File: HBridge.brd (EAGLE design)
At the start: 59.7 x 53.3 mm, 42 parts, among them IC1 74HC08D, IC2 A4954, J1 In 1/2, J2 In 3/4

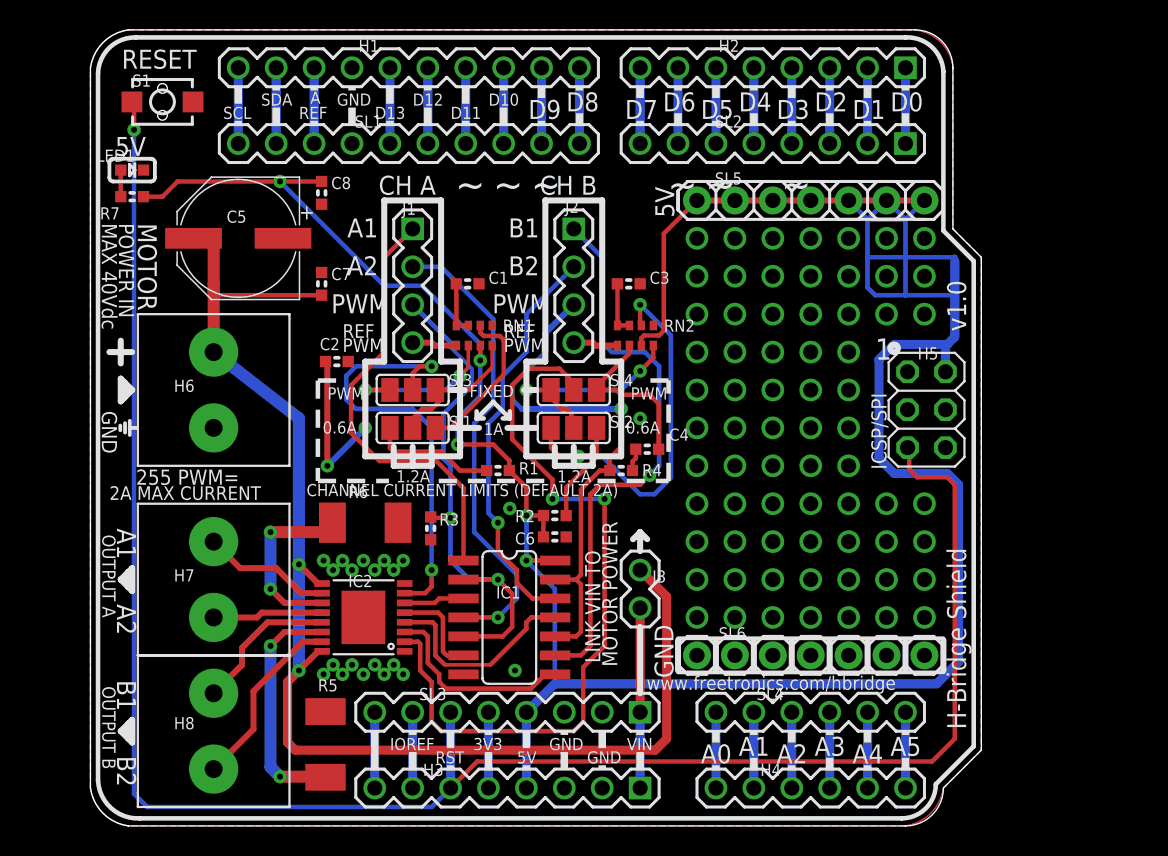
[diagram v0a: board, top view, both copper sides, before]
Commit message: Restructured schematic and board for switchable current limit
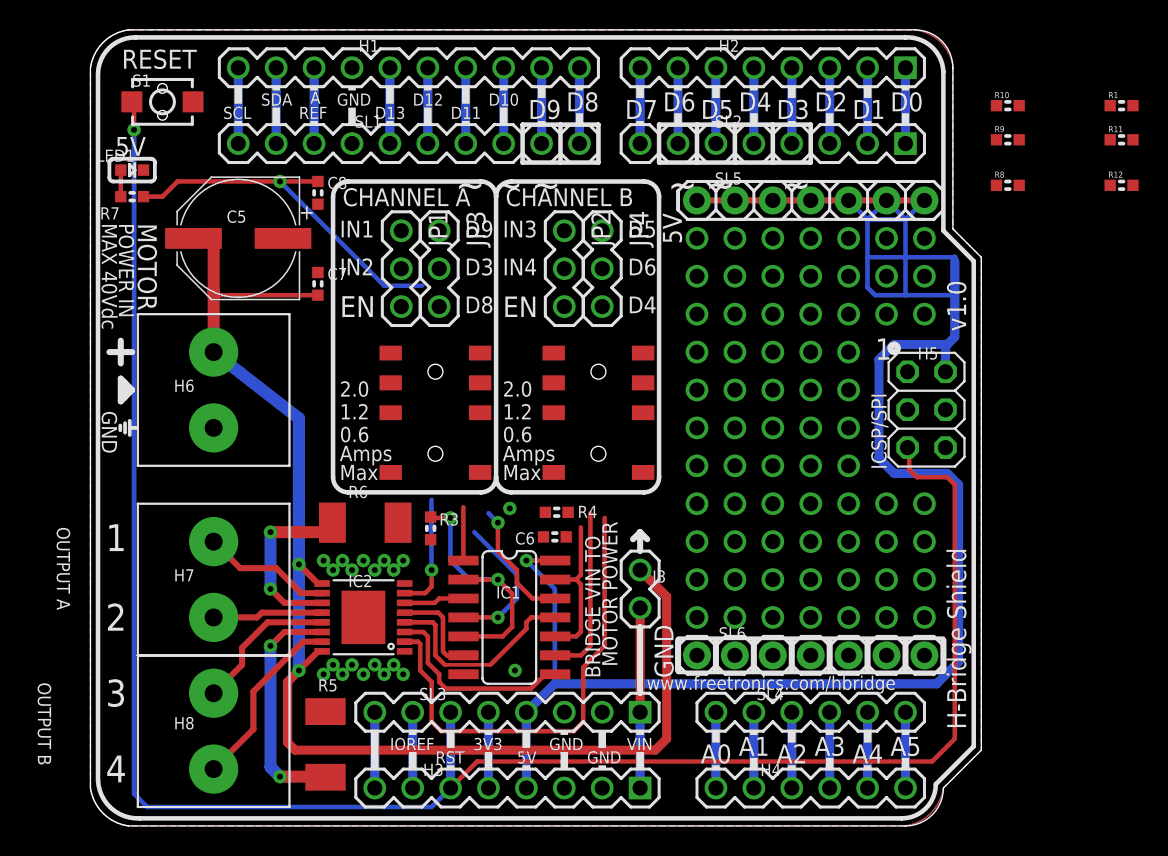
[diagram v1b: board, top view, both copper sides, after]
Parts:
- removed C1, C2, C3, C4: 100nF, freetronics-master-v1:0603
- removed J1: In 1/2, freetronics-master-v1:1X04
- removed J2: In 3/4, freetronics-master-v1:1X04
- removed R2: 2K2, freetronics-master-v1:0603
- removed RN1, RN2: 1K, freetronics-master-v1:CAY16
- removed SJ1: Ch1 Fixed Current Select, freetronics-master-v1:SJ_2
- removed SJ2: Ch2 Fixed Current Select, freetronics-master-v1:SJ_2
- removed SJ3: Ch1 Fixed/PWM select, freetronics-master-v1:SJ_2
- removed SJ4: Ch2 Fixed/PWM select, freetronics-master-v1:SJ_2
- added JP1, JP2, JP3, JP4: (no value), freetronics-master-v1.1:1X03
- added R10: 3K3, freetronics-master-v1:0603
- added R11, R9: 953R, freetronics-master-v1:0603
- added R12, R8: 2K2, freetronics-master-v1:0603
- added SW1, SW2: SWITCH-DP3T, freetronics-jon:MS-23C01
- R1: value 2K2 -> 3K3
- moved R1 48.4 mm to (69.1, 48.3)
- moved R4 5.14 mm to (31.2, 21.0)
- moved C7 0.25 mm to (15.2, 36.3)
- moved C8 0.25 mm to (15.2, 42.4)
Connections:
- removed net N$1: RN2.4, SJ2.2, SJ4.3
- removed net N$16: RN1.4, SJ1.2, SJ3.3
- removed net N$17: R2.1, SJ2.1
- removed net N$18: C2.1, RN1.2, SJ3.1
- removed net N$19: C1.1, RN1.7, RN1.8
- removed net N$2: C4.1, RN2.2, SJ4.1
- removed net N$20: RN2.6, SJ2.3
- removed net N$3: C3.1, RN2.7, RN2.8
- removed net PWM12: IC1.2, IC1.5, J1.3, R3.2
- removed net PWM34: IC1.10, IC1.13, J2.3, R4.2
- removed net REF_PWM_12: J1.4, RN1.1
- removed net REF_PWM_34: J2.4, RN2.1
- new net EN-A: IC1.2, IC1.5, JP1.3, R3.2
- new net EN-B: IC1.10, IC1.13, JP2.3, R4.1
- new net N$21: R9.1, SW1.2-3
- new net N$49: R1.1, SW2.2-2
- net +5V: now also R12.1, R3.1, R4.2, R8.1; no longer R1.2, R2.2, RN1.3, RN2.3
- net D3: now also JP3.2
- net D4: now also JP4.3
- net D5: now also JP4.1
- net D6: now also JP4.2
- net D8: now also JP3.3
- net D9: now also JP3.1
- net GND: now also R1.2, R10.2, R11.2, R9.2; no longer C1.2, C2.2, C3.2, C4.2, R3.1, R4.1, RN1.5, RN2.5
- net IN1: now also JP1.1; no longer J1.1
- net IN2: now also JP1.2; no longer J1.2
- net IN3: now also JP2.1; no longer J2.1
- net IN4: now also JP2.2; no longer J2.2
- net N$15: now also R10.1, SW1.2-2; no longer RN1.6, SJ1.3
- net N$4: now also R11.1, SW2.2-3; no longer R1.1, SJ1.1
- net VREF12: now also R8.2, SW1.2-C; no longer SJ3.2
- net VREF34: now also R12.2, SW2.2-C; no longer SJ4.2
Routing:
- net +5V: track 194.5 -> 154.9 mm, vias 5 -> 2
- net PWM12: track 35.6 -> 0.00 mm, vias 2 -> 0
- net PWM34: track 35.6 -> 0.00 mm, vias 1 -> 0
- net IN3: track 37.7 -> 11.5 mm, vias 1 -> 0
- net IN1: track 29.3 -> 3.58 mm
- net N$20: track 25.0 -> 0.00 mm, vias 2 -> 0
- net N$18: track 23.9 -> 0.00 mm, vias 4 -> 0
- net IN2: track 31.4 -> 9.74 mm
- net VREF12: track 29.3 -> 7.80 mm, vias 2 -> 1
- net VREF34: track 50.5 -> 31.6 mm, vias 2 -> 0
- net IN4: track 27.3 -> 8.46 mm
- net EN-A: track 0.00 -> 18.7 mm, vias 0 -> 2
- net N$1: track 15.2 -> 0.00 mm, vias 2 -> 0
- net N$2: track 11.8 -> 0.00 mm
- net N$15: track 10.6 -> 0.00 mm
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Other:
- board text added: "0.6"
- board text added: "1.2"
- board text added: "2"
- board text added: "2.0"
- board text added: "3"
- board text added: "4"
- board text added: "Amps"
- board text added: "BRIDGE VIN TO"
- board text added: "CHANNEL A"
- board text added: "CHANNEL B"
- board text added: "EN"
- board text added: "IN1"
- board text added: "IN2"
- board text added: "IN3"
- board text added: "IN4"
- board text added: "Max"
- board text removed: "0.6A"
- board text removed: "1.2A"
- board text removed: "1A"
- board text removed: "255 PWM="
- board text removed: "2A MAX CURRENT"
- board text removed: "B1"
- board text removed: "B2"
- board text removed: "CH A"
- board text removed: "CH B"
- board text removed: "CHANNEL CURRENT LIMITS (DEFAULT 2A)"
- board text removed: "FIXED"
- board text removed: "LINK VIN TO"
- board text removed: "PWM"

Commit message: Changed input pins; rerouted; ERC and DRC
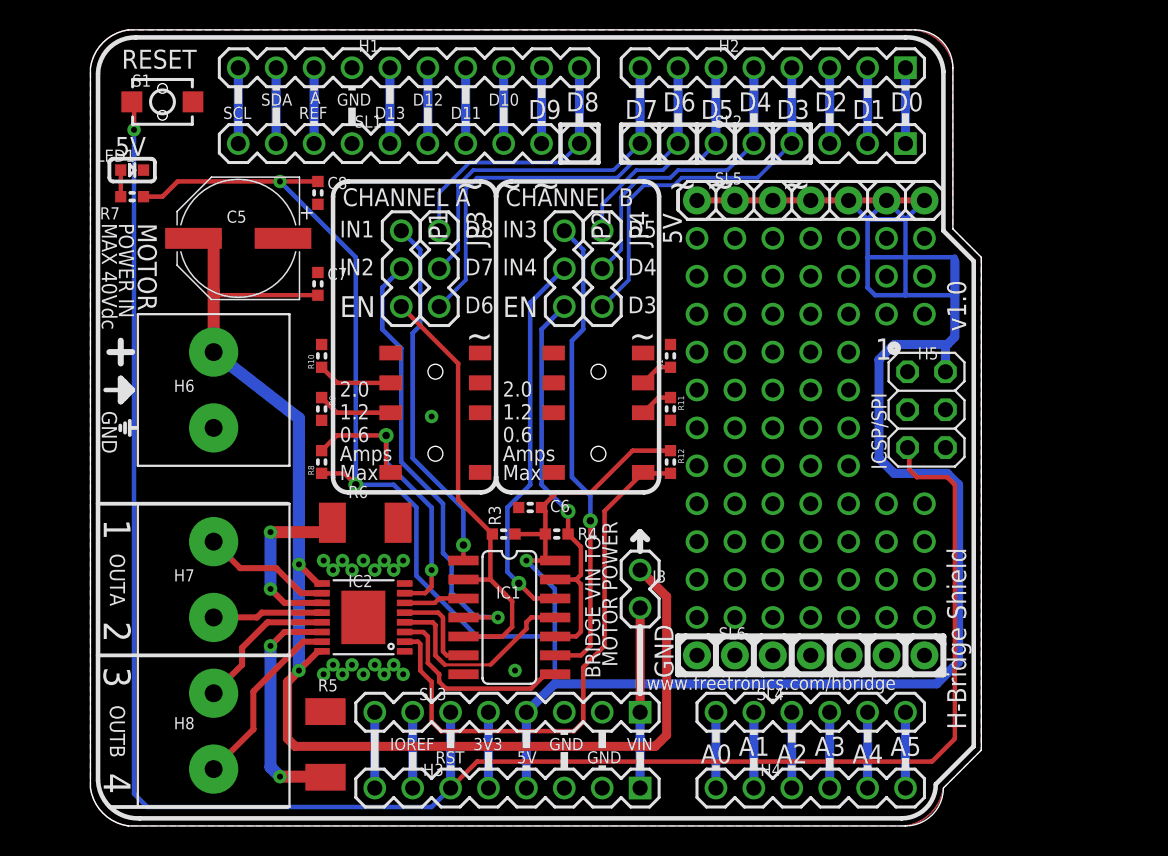
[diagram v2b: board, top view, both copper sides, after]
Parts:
- moved R8 49.6 mm to (15.5, 24.4), turned to 90 degrees
- moved R9 49.4 mm to (15.5, 27.9), turned to 270 degrees
- moved R10 48.9 mm to (15.5, 31.5), turned to 90 degrees
- moved R12 35.5 mm to (38.9, 24.4), turned to 270 degrees
- moved R11 35.2 mm to (38.9, 27.9), turned to 270 degrees
- moved R1 34.6 mm to (38.9, 31.5), turned to 90 degrees
- moved R3 4.90 mm to (27.7, 19.6), turned to 180 degrees
- moved C6 2.57 mm to (29.5, 21.3), turned to 180 degrees
- moved R4 1.46 mm to (31.2, 19.6)
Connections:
- net D3: now also JP4.3; no longer JP3.2
- net D4: now also JP4.2; no longer JP4.3
- net D6: now also JP3.3; no longer JP4.2
- net D7: now also JP3.2
- net D8: now also JP3.1; no longer JP3.3
- net D9: no longer JP3.1
- net N$15: now also SW1.1-2; no longer SW1.2-2
- net N$21: now also SW1.1-3; no longer SW1.2-3
- net VREF12: now also SW1.1-C; no longer SW1.2-C
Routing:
- net +5V: track 154.9 -> 203.6 mm, vias 2 -> 3
- net D6: track 5.08 -> 29.2 mm
- net IN1: track 3.58 -> 24.2 mm, vias 0 -> 1
- net IN2: track 9.74 -> 30.2 mm
- net D3: track 5.08 -> 25.4 mm
- net IN3: track 11.5 -> 31.8 mm, vias 0 -> 1
- net D7: track 5.08 -> 24.5 mm
- net IN4: track 8.46 -> 25.8 mm
- net EN-B: track 10.5 -> 27.0 mm, vias 0 -> 1
- net D4: track 5.08 -> 20.8 mm
- net D8: track 5.08 -> 18.4 mm
- net VREF12: track 7.80 -> 20.7 mm, vias 1 -> 2
- net EN-A: track 18.7 -> 31.3 mm, vias 2 -> 0
- net D5: track 5.08 -> 16.2 mm
- net VREF34: track 31.6 -> 37.5 mm
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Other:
- board text added: "OUTA"
- board text added: "OUTB"
- board text removed: "OUTPUT A"
- board text removed: "OUTPUT B"

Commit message: Annotation updates for release
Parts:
- removed J3: (no value), freetronics-master-v1:1X02
- removed JP4: (no value), freetronics-master-v1.1:1X03
- removed R12: 2K2, freetronics-master-v1:0603
- removed SW1: SWITCH-DP3T, freetronics-jon:MS-23C01
- added R2: 10K 0603, freetronics-master-v1:0603
- added S3: RESET, freetronics-master-v1:TACTILE_SWITCH_SMD_2PIN_TINY
- C1, C4: value 100nF -> 100nF 0603
- C2: value 100uF -> 100uF 50V
- C3: value 220nF -> 220nF 50V 0603
- IC1: value 74HC08D -> 74HC08D SOIC-14
- IC2: value A4954 -> A4954 TSSOP-16
- JP1, JP2: device freetronics-master-v1.1:1X03 -> freetronics-master-v1:2X03
- JP3: device freetronics-master-v1.1:1X03 -> freetronics-master-v1:1X02
- R1: value 3K3 -> 10K 0603
- R10: value 3K3 -> 0.25R 1W 2010; device freetronics-master-v1:0603 -> rcl:R2010
- R11: value 953R -> 2K2 0603; device freetronics-master-v1:0603 -> freetronics:0603
- R3: value 10K -> 2K2 0603
- R4: value 10K -> 3K3 1% 0603
- R5: value 0.25R 1W -> 953R 1% 0603; device rcl:R2010 -> freetronics-master-v1:0603
- R6: value 0.25R 1W -> 2K2 0603; device rcl:R2010 -> freetronics-master-v1:0603
- R7: value 2K2 -> 3K3 1% 0603; device freetronics:0603 -> freetronics-master-v1:0603
- R8: value 2K2 -> 953R 1% 0603
- R9: value 953R -> 0.25R 1W 2010; device freetronics-master-v1:0603 -> rcl:R2010
- S1: value RESET -> SWITCH-DP3T MS-23C01; device freetronics-master-v1:TACTILE_SWITCH_SMD_2PIN_TINY -> freetronics-jon:MS-23C01
- S2: value SWITCH-DP3T -> SWITCH-DP3T MS-23C01
- moved R11 38.8 mm to (2.79, 42.2), turned to 180 degrees
- moved R7 37.6 mm to (38.9, 31.5), turned to 90 degrees
- moved JP3 28.6 mm to (36.8, 14.6), turned to 90 degrees
- moved S1 27.7 mm to (23.1, 27.7)
- moved R8 23.4 mm to (38.9, 22.9), turned to 270 degrees
- moved R9 22.5 mm to (15.7, 5.46)
- moved R6 21.5 mm to (38.9, 26.9), turned to 90 degrees
- moved R4 19.8 mm to (15.5, 31.5), turned to 90 degrees
- moved R5 18.9 mm to (15.5, 24.4), turned to 90 degrees
- moved R1 16.4 mm to (27.7, 19.6), turned to 180 degrees
- moved R3 14.8 mm to (15.5, 27.9), turned to 270 degrees
- moved R10 11.6 mm to (18.4, 20.3), turned to 180 degrees
- moved JP2 2.84 mm to (33.0, 37.3)
- moved JP1 2.84 mm to (22.1, 37.3)
- renumbered C5 to C2, C6 to C1, C7 to C3, C8 to C4, SW2 to S2
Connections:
- net +5V: now also R1.1, R11.1, R2.2, R6.1; no longer R12.1, R4.2, R7.1, R8.1
- net D2: now also JP2.4
- net D3: now also JP2.2; no longer JP4.3
- net D4: now also JP1.2; no longer JP4.2
- net D5: now also JP2.6; no longer JP4.1
- net D6: now also JP1.6; no longer JP3.3
- net D7: now also JP1.4; no longer JP3.2
- net D8: no longer JP3.1
- net EN-A: now also JP1.5, R1.2; no longer JP1.3, R3.2
- net EN-B: now also JP2.5, R2.1; no longer JP2.3, R4.1
- net GND: now also R10.1, R4.2, R5.2, R7.2, R8.2, R9.1, S3.2; no longer R1.2, R10.2, R11.2, R5.1, R6.1, R9.2, S1.2
- net IN2: now also JP1.3; no longer JP1.2
- net IN4: now also JP2.3; no longer JP2.2
- net N$13: now also R9.2; no longer R5.2
- net N$14: now also R10.2; no longer R6.2
- net N$15: now also R4.1, S1.1-2; no longer R10.1, SW1.1-2
- net N$21: now also R5.1, S1.1-3; no longer R9.1, SW1.1-3
- net N$22: now also R11.2; no longer R7.2
- net N$4: now also R8.1; no longer R11.1
- net N$49: now also R7.1; no longer R1.1
- net RESET: now also S3.1; no longer S1.1
- net VBB: now also JP3.2; no longer J3.2
- net VIN: now also JP3.1; no longer J3.1
- net VREF12: now also R3.2, S1.1-C; no longer R8.2, SW1.1-C
- net VREF34: now also R6.2; no longer R12.2
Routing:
- net +5V: track 203.6 -> 177.5 mm
- net D2: track 5.08 -> 25.4 mm
- net D4: track 20.8 -> 38.3 mm
- net D8: track 18.4 -> 5.08 mm
- net D5: track 16.2 -> 22.6 mm, vias 0 -> 1
- net D3: track 25.4 -> 20.8 mm
- net VREF34: track 37.5 -> 41.5 mm, vias 0 -> 2
- net VREF12: track 20.7 -> 19.8 mm
- net D7: track 24.5 -> 23.8 mm
- net D6: track 29.2 -> 28.4 mm
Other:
- board text added: "(c) 2013 Freetronics Pty Ltd"
- board text added: "H-Bridge Motor Controller Shield"
- board text added: "K"
- board text added: "OUT A"
- board text added: "OUT B"
- board text added: "R3"
- board text added: "S2"
- board text added: "S3"
- board text added: "V1.1"
- board text added: "v1.1"
- board text removed: "(c) 2012 Freetronics Pty Ltd"
- board text removed: "H-Bridge Motor Controller"
- board text removed: "OUTA"
- board text removed: "OUTB"
- board text removed: "V1.0"
- board text removed: "v1.0"

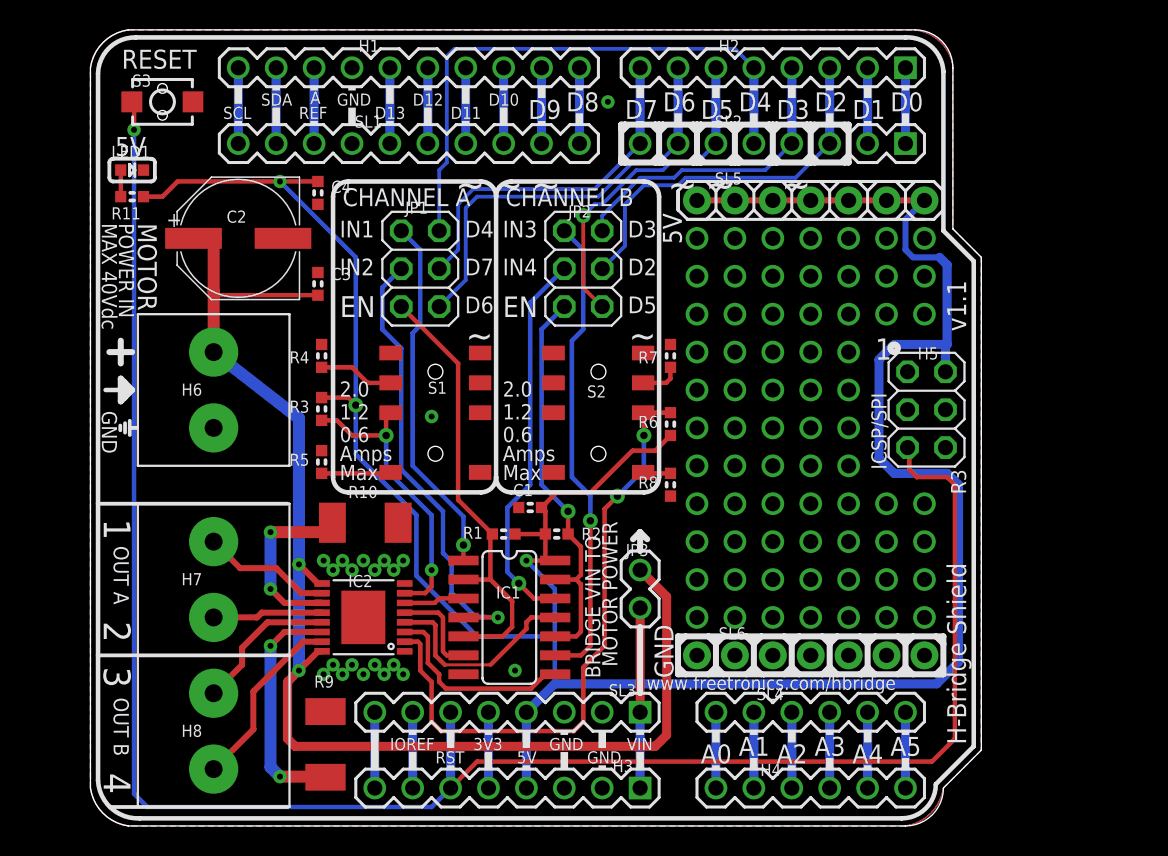
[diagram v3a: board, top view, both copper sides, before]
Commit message: Version 1.2: 3.3V compatibility via the IORef pin on Arduino R3
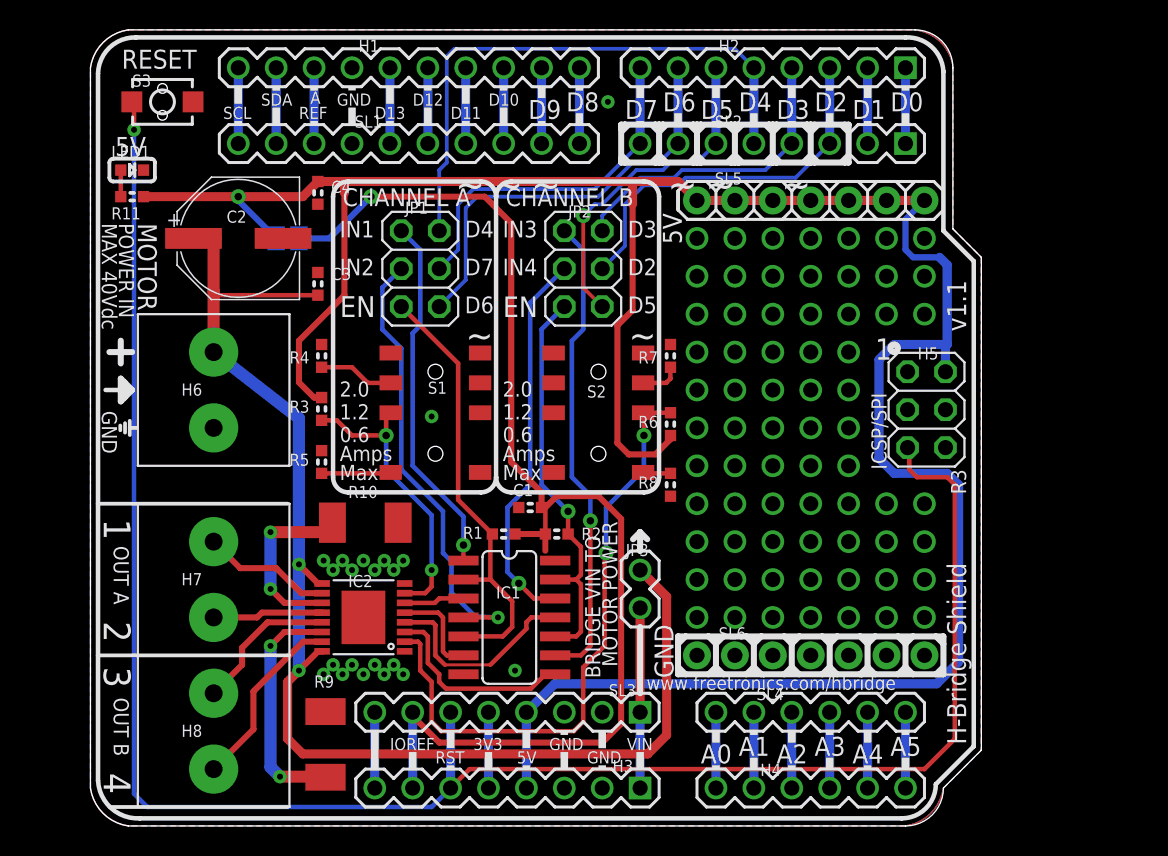
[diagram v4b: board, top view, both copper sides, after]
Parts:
- added SJ1: (no value), freetronics-master-v1.1:SJ
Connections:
- net +5V: now also SJ1.2; no longer C1.1, IC1.14, R1.1, R2.2
- net IOREF: now also C1.1, IC1.14, R1.1, R2.2, SJ1.1
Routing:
- net IOREF: track 5.08 -> 81.5 mm, vias 0 -> 1
- net +5V: track 177.5 -> 175.5 mm, vias 3 -> 1
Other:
- board text added: "3.3V"
- board text added: "COMPATIBLE"
- board text added: "IOREF-5V"
- board text added: "V1.2"
- board text removed: "V1.1"
